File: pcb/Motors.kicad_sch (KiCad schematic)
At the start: 10 parts, among them M1 LEFT, M2 RIGHT, U11 TB6612FNG

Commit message: [pcb] 4 layer PCB
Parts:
- renumbered U11 to U12
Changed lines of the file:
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@@
   (symbol (lib_id "power:+3.3V") (at 46.99 58.42 0) (unit 1)
     (in_bom yes) (on_board yes) (dnp no) (fields_autoplaced)
-    (property "Reference" "#PWR042" (at 46.99 62.23 0)
+    (property "Reference" "#PWR043" (at 46.99 62.23 0)
       (effects (font (size 1.27 1.27)) hide)
     )
@@
       (project "Autko"
         (path "/8d5cfdec-de34-4148-9100-7125640c46f5/541574ca-21e4-445f-b8e2-ded2c59d3b8a"
-          (reference "#PWR042") (unit 1)
+          (reference "#PWR043") (unit 1)
         )
       )
@@
   (symbol (lib_id "Driver_Motor:TB6612FNG") (at 64.77 69.85 0) (unit 1)
     (in_bom yes) (on_board yes) (dnp no) (fields_autoplaced)
-    (property "Reference" "U11" (at 74.3459 92.71 0)
+    (property "Reference" "U12" (at 74.3459 92.71 0)
       (effects (font (size 1.27 1.27)) (justify left))
     )
@@
       (project "Autko"
         (path "/8d5cfdec-de34-4148-9100-7125640c46f5/541574ca-21e4-445f-b8e2-ded2c59d3b8a"
-          (reference "U11") (unit 1)
+          (reference "U12") (unit 1)
         )
       )
@@
   (symbol (lib_id "power:GND") (at 90.17 44.45 0) (unit 1)
     (in_bom yes) (on_board yes) (dnp no)
-    (property "Reference" "#PWR041" (at 90.17 50.8 0)
+    (property "Reference" "#PWR042" (at 90.17 50.8 0)
       (effects (font (size 1.27 1.27)) hide)
     )
@@
       (project "Autko"
         (path "/8d5cfdec-de34-4148-9100-7125640c46f5/541574ca-21e4-445f-b8e2-ded2c59d3b8a"
+          (reference "#PWR042") (unit 1)
+        )
+      )
+    )
+  )
+  (symbol (lib_id "power:+3.3V") (at 46.99 31.75 0) (unit 1)
+    (in_bom yes) (on_board yes) (dnp no) (fields_autoplaced)
+    (property "Reference" "#PWR039" (at 46.99 35.56 0)
+      (effects (font (size 1.27 1.27)) hide)
+    )
+    (property "Value" "+3.3V" (at 46.99 27.94 0)
+      (effects (font (size 1.27 1.27)))
+    )
+    (property "Footprint" "" (at 46.99 31.75 0)
+      (effects (font (size 1.27 1.27)) hide)
+    )
+    (property "Datasheet" "" (at 46.99 31.75 0)
+      (effects (font (size 1.27 1.27)) hide)
+    )
+    (pin "1")
+    (instances
+      (project "Autko"
+        (path "/8d5cfdec-de34-4148-9100-7125640c46f5/541574ca-21e4-445f-b8e2-ded2c59d3b8a"
+          (reference "#PWR039") (unit 1)
+        )
+      )
+    )
+  )
+  (symbol (lib_id "power:+7.5V") (at 90.17 31.75 0) (unit 1)
+    (in_bom yes) (on_board yes) (dnp no) (fields_autoplaced)
+    (property "Reference" "#PWR040" (at 90.17 35.56 0)
+      (effects (font (size 1.27 1.27)) hide)
+    )
+    (property "Value" "+7.5V" (at 90.17 27.94 0)
+      (effects (font (size 1.27 1.27)))
+    )
+    (property "Footprint" "" (at 90.17 31.75 0)
+      (effects (font (size 1.27 1.27)) hide)
+    )
+    (property "Datasheet" "" (at 90.17 31.75 0)
+      (effects (font (size 1.27 1.27)) hide)
+    )
+    (pin "1")
+    (instances
+      (project "Autko"
+        (path "/8d5cfdec-de34-4148-9100-7125640c46f5/541574ca-21e4-445f-b8e2-ded2c59d3b8a"
+          (reference "#PWR040") (unit 1)
+        )
+      )
+    )
+  )
+  (symbol (lib_id "Device:C") (at 92.71 59.69 0) (mirror y) (unit 1)
+    (in_bom yes) (on_board yes) (dnp no)
+    (property "Reference" "C22" (at 90.17 58.42 0)
+      (effects (font (size 1.27 1.27)) (justify left))
+    )
+    (property "Value" "100nF" (at 90.17 60.96 0)
+      (effects (font (size 1.27 1.27)) (justify left))
+    )
+    (property "Footprint" "Capacitor_SMD:C_0805_2012Metric" (at 91.7448 63.5 0)
+      (effects (font (size 1.27 1.27)) hide)
+    )
+    (property "Datasheet" "~" (at 92.71 59.69 0)
+      (effects (font (size 1.27 1.27)) hide)
+    )
+    (pin "1")
+    (pin "2")
+    (instances
+      (project "Autko"
+        (path "/8d5cfdec-de34-4148-9100-7125640c46f5/541574ca-21e4-445f-b8e2-ded2c59d3b8a"
+          (reference "C22") (unit 1)
+        )
+      )
+    )
+  )
+  (symbol (lib_id "Device:C") (at 77.47 38.1 0) (unit 1)
+    (in_bom yes) (on_board yes) (dnp no)
+    (property "Reference" "C20" (at 80.01 36.83 0)
+      (effects (font (size 1.27 1.27)) (justify left))
+    )
+    (property "Value" "100nF" (at 80.01 39.37 0)
+      (effects (font (size 1.27 1.27)) (justify left))
+    )
+    (property "Footprint" "Capacitor_SMD:C_0805_2012Metric" (at 78.4352 41.91 0)
+      (effects (font (size 1.27 1.27)) hide)
+    )
+    (property "Datasheet" "~" (at 77.47 38.1 0)
+      (effects (font (size 1.27 1.27)) hide)
+    )
+    (pin "1")
+    (pin "2")
+    (instances
+      (project "Autko"
+        (path "/8d5cfdec-de34-4148-9100-7125640c46f5/541574ca-21e4-445f-b8e2-ded2c59d3b8a"
+          (reference "C20") (unit 1)
+        )
+      )
+    )
+  )
+  (symbol (lib_id "power:GND") (at 46.99 44.45 0) (unit 1)
+    (in_bom yes) (on_board yes) (dnp no)
+    (property "Reference" "#PWR041" (at 46.99 50.8 0)
+      (effects (font (size 1.27 1.27)) hide)
+    )
+    (property "Value" "GND" (at 46.99 48.26 0)
+      (effects (font (size 1.27 1.27)))
+    )
+    (property "Footprint" "" (at 46.99 44.45 0)
+      (effects (font (size 1.27 1.27)) hide)
+    )
+    (property "Datasheet" "" (at 46.99 44.45 0)
+      (effects (font (size 1.27 1.27)) hide)
+    )
+    (pin "1")
+    (instances
+      (project "Autko"
+        (path "/8d5cfdec-de34-4148-9100-7125640c46f5/541574ca-21e4-445f-b8e2-ded2c59d3b8a"
           (reference "#PWR041") (unit 1)
         )
@@
     )
   )
-  (symbol (lib_id "power:+3.3V") (at 46.99 31.75 0) (unit 1)
-    (in_bom yes) (on_board yes) (dnp no) (fields_autoplaced)
-    (property "Reference" "#PWR038" (at 46.99 35.56 0)
-      (effects (font (size 1.27 1.27)) hide)
-    )
-    (property "Value" "+3.3V" (at 46.99 27.94 0)
-      (effects (font (size 1.27 1.27)))
-    )
-    (property "Footprint" "" (at 46.99 31.75 0)
-      (effects (font (size 1.27 1.27)) hide)
-    )
-    (property "Datasheet" "" (at 46.99 31.75 0)
-      (effects (font (size 1.27 1.27)) hide)
-    )
-    (pin "1")
-    (instances
-      (project "Autko"
-        (path "/8d5cfdec-de34-4148-9100-7125640c46f5/541574ca-21e4-445f-b8e2-ded2c59d3b8a"
-          (reference "#PWR038") (unit 1)
-        )
-      )
-    )
-  )
-  (symbol (lib_id "power:+7.5V") (at 90.17 31.75 0) (unit 1)
-    (in_bom yes) (on_board yes) (dnp no) (fields_autoplaced)
-    (property "Reference" "#PWR039" (at 90.17 35.56 0)
-      (effects (font (size 1.27 1.27)) hide)
-    )
-    (property "Value" "+7.5V" (at 90.17 27.94 0)
-      (effects (font (size 1.27 1.27)))
-    )
-    (property "Footprint" "" (at 90.17 31.75 0)
-      (effects (font (size 1.27 1.27)) hide)
-    )
-    (property "Datasheet" "" (at 90.17 31.75 0)
-      (effects (font (size 1.27 1.27)) hide)
-    )
-    (pin "1")
-    (instances
-      (project "Autko"
-        (path "/8d5cfdec-de34-4148-9100-7125640c46f5/541574ca-21e4-445f-b8e2-ded2c59d3b8a"
-          (reference "#PWR039") (unit 1)
-        )
-      )
-    )
-  )
-  (symbol (lib_id "Device:C") (at 92.71 59.69 0) (mirror y) (unit 1)
-    (in_bom yes) (on_board yes) (dnp no)
-    (property "Reference" "C22" (at 90.17 58.42 0)
-      (effects (font (size 1.27 1.27)) (justify left))
-    )
-    (property "Value" "100nF" (at 90.17 60.96 0)
-      (effects (font (size 1.27 1.27)) (justify left))
-    )
-    (property "Footprint" "Capacitor_SMD:C_0805_2012Metric" (at 91.7448 63.5 0)
-      (effects (font (size 1.27 1.27)) hide)
-    )
-    (property "Datasheet" "~" (at 92.71 59.69 0)
-      (effects (font (size 1.27 1.27)) hide)
-    )
-    (pin "1")
-    (pin "2")
-    (instances
-      (project "Autko"
-        (path "/8d5cfdec-de34-4148-9100-7125640c46f5/541574ca-21e4-445f-b8e2-ded2c59d3b8a"
-          (reference "C22") (unit 1)
-        )
-      )
-    )
-  )
-  (symbol (lib_id "Device:C") (at 77.47 38.1 0) (unit 1)
-    (in_bom yes) (on_board yes) (dnp no)
-    (property "Reference" "C20" (at 80.01 36.83 0)
-      (effects (font (size 1.27 1.27)) (justify left))
-    )
-    (property "Value" "100nF" (at 80.01 39.37 0)
-      (effects (font (size 1.27 1.27)) (justify left))
-    )
-    (property "Footprint" "Capacitor_SMD:C_0805_2012Metric" (at 78.4352 41.91 0)
-      (effects (font (size 1.27 1.27)) hide)
-    )
-    (property "Datasheet" "~" (at 77.47 38.1 0)
-      (effects (font (size 1.27 1.27)) hide)
-    )
-    (pin "1")
-    (pin "2")
-    (instances
-      (project "Autko"
-        (path "/8d5cfdec-de34-4148-9100-7125640c46f5/541574ca-21e4-445f-b8e2-ded2c59d3b8a"
-          (reference "C20") (unit 1)
-        )
-      )
-    )
-  )
-  (symbol (lib_id "power:GND") (at 46.99 44.45 0) (unit 1)
-    (in_bom yes) (on_board yes) (dnp no)
-    (property "Reference" "#PWR040" (at 46.99 50.8 0)
-      (effects (font (size 1.27 1.27)) hide)
-    )
-    (property "Value" "GND" (at 46.99 48.26 0)
-      (effects (font (size 1.27 1.27)))
-    )
-    (property "Footprint" "" (at 46.99 44.45 0)
-      (effects (font (size 1.27 1.27)) hide)
-    )
-    (property "Datasheet" "" (at 46.99 44.45 0)
-      (effects (font (size 1.27 1.27)) hide)
-    )
-    (pin "1")
-    (instances
-      (project "Autko"
-        (path "/8d5cfdec-de34-4148-9100-7125640c46f5/541574ca-21e4-445f-b8e2-ded2c59d3b8a"
-          (reference "#PWR040") (unit 1)
-        )
-      )
-    )
-  )
   (symbol (lib_id "power:GND") (at 67.31 97.79 0) (unit 1)
     (in_bom yes) (on_board yes) (dnp no)
-    (property "Reference" "#PWR043" (at 67.31 104.14 0)
+    (property "Reference" "#PWR044" (at 67.31 104.14 0)
       (effects (font (size 1.27 1.27)) hide)
     )
@@
       (project "Autko"
         (path "/8d5cfdec-de34-4148-9100-7125640c46f5/541574ca-21e4-445f-b8e2-ded2c59d3b8a"
-          (reference "#PWR043") (unit 1)
-        )
-      )
+          (reference "#PWR044") (unit 1)
+        )
+      )

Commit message: [pcb] BT config rework
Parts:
- renumbered TP15 to TP14, TP16 to TP15, U12 to U11
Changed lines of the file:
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@@
   (symbol (lib_id "Connector:TestPoint") (at 35.56 68.58 180) (unit 1)
     (in_bom yes) (on_board yes) (dnp no)
-    (property "Reference" "TP16" (at 35.56 73.66 0)
+    (property "Reference" "TP15" (at 35.56 73.66 0)
       (effects (font (size 1.27 1.27)))
     )
@@
       (project "Autko"
         (path "/8d5cfdec-de34-4148-9100-7125640c46f5/541574ca-21e4-445f-b8e2-ded2c59d3b8a"
-          (reference "TP16") (unit 1)
+          (reference "TP15") (unit 1)
         )
       )
@@
   (symbol (lib_id "Connector:TestPoint") (at 35.56 63.5 0) (unit 1)
     (in_bom yes) (on_board yes) (dnp no)
-    (property "Reference" "TP15" (at 35.56 58.42 0)
+    (property "Reference" "TP14" (at 35.56 58.42 0)
       (effects (font (size 1.27 1.27)))
     )
@@
       (project "Autko"
         (path "/8d5cfdec-de34-4148-9100-7125640c46f5/541574ca-21e4-445f-b8e2-ded2c59d3b8a"
-          (reference "TP15") (unit 1)
+          (reference "TP14") (unit 1)
         )
       )
@@
   (symbol (lib_id "power:+3.3V") (at 46.99 58.42 0) (unit 1)
     (in_bom yes) (on_board yes) (dnp no) (fields_autoplaced)
-    (property "Reference" "#PWR043" (at 46.99 62.23 0)
+    (property "Reference" "#PWR048" (at 46.99 62.23 0)
       (effects (font (size 1.27 1.27)) hide)
     )
@@
       (project "Autko"
         (path "/8d5cfdec-de34-4148-9100-7125640c46f5/541574ca-21e4-445f-b8e2-ded2c59d3b8a"
-          (reference "#PWR043") (unit 1)
+          (reference "#PWR048") (unit 1)
         )
       )
@@
   (symbol (lib_id "Driver_Motor:TB6612FNG") (at 64.77 69.85 0) (unit 1)
     (in_bom yes) (on_board yes) (dnp no) (fields_autoplaced)
-    (property "Reference" "U12" (at 74.3459 92.71 0)
+    (property "Reference" "U11" (at 74.3459 92.71 0)
       (effects (font (size 1.27 1.27)) (justify left))
     )
@@
       (project "Autko"
         (path "/8d5cfdec-de34-4148-9100-7125640c46f5/541574ca-21e4-445f-b8e2-ded2c59d3b8a"
-          (reference "U12") (unit 1)
+          (reference "U11") (unit 1)
         )
       )
@@
   (symbol (lib_id "power:GND") (at 90.17 44.45 0) (unit 1)
     (in_bom yes) (on_board yes) (dnp no)
-    (property "Reference" "#PWR042" (at 90.17 50.8 0)
+    (property "Reference" "#PWR047" (at 90.17 50.8 0)
       (effects (font (size 1.27 1.27)) hide)
     )
@@
       (project "Autko"
         (path "/8d5cfdec-de34-4148-9100-7125640c46f5/541574ca-21e4-445f-b8e2-ded2c59d3b8a"
-          (reference "#PWR042") (unit 1)
+          (reference "#PWR047") (unit 1)
         )
       )
@@
   (symbol (lib_id "power:+3.3V") (at 46.99 31.75 0) (unit 1)
     (in_bom yes) (on_board yes) (dnp no) (fields_autoplaced)
-    (property "Reference" "#PWR039" (at 46.99 35.56 0)
+    (property "Reference" "#PWR044" (at 46.99 35.56 0)
       (effects (font (size 1.27 1.27)) hide)
     )
@@
       (project "Autko"
         (path "/8d5cfdec-de34-4148-9100-7125640c46f5/541574ca-21e4-445f-b8e2-ded2c59d3b8a"
-          (reference "#PWR039") (unit 1)
+          (reference "#PWR044") (unit 1)
         )
       )
@@
   (symbol (lib_id "power:+7.5V") (at 90.17 31.75 0) (unit 1)
     (in_bom yes) (on_board yes) (dnp no) (fields_autoplaced)
-    (property "Reference" "#PWR040" (at 90.17 35.56 0)
+    (property "Reference" "#PWR045" (at 90.17 35.56 0)
       (effects (font (size 1.27 1.27)) hide)
     )
@@
       (project "Autko"
         (path "/8d5cfdec-de34-4148-9100-7125640c46f5/541574ca-21e4-445f-b8e2-ded2c59d3b8a"
-          (reference "#PWR040") (unit 1)
+          (reference "#PWR045") (unit 1)
         )
       )
@@
   (symbol (lib_id "power:GND") (at 46.99 44.45 0) (unit 1)
     (in_bom yes) (on_board yes) (dnp no)
-    (property "Reference" "#PWR041" (at 46.99 50.8 0)
+    (property "Reference" "#PWR046" (at 46.99 50.8 0)
       (effects (font (size 1.27 1.27)) hide)
     )
@@
       (project "Autko"
         (path "/8d5cfdec-de34-4148-9100-7125640c46f5/541574ca-21e4-445f-b8e2-ded2c59d3b8a"
-          (reference "#PWR041") (unit 1)
+          (reference "#PWR046") (unit 1)
         )
       )
@@
   (symbol (lib_id "power:GND") (at 67.31 97.79 0) (unit 1)
     (in_bom yes) (on_board yes) (dnp no)
-    (property "Reference" "#PWR044" (at 67.31 104.14 0)
+    (property "Reference" "#PWR049" (at 67.31 104.14 0)
       (effects (font (size 1.27 1.27)) hide)
     )
@@
       (project "Autko"
         (path "/8d5cfdec-de34-4148-9100-7125640c46f5/541574ca-21e4-445f-b8e2-ded2c59d3b8a"
-          (reference "#PWR044") (unit 1)
-        )
-      )
+          (reference "#PWR049") (unit 1)
+        )
+      )

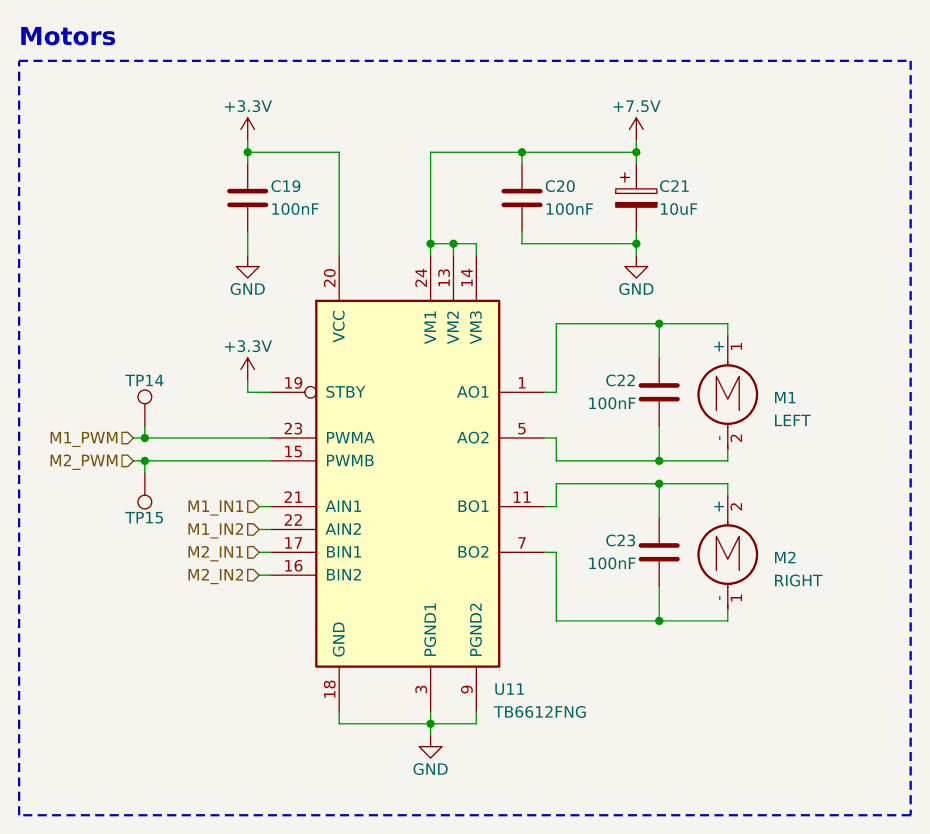
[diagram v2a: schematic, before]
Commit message: [pcb] More final touches, UART test ponts added.
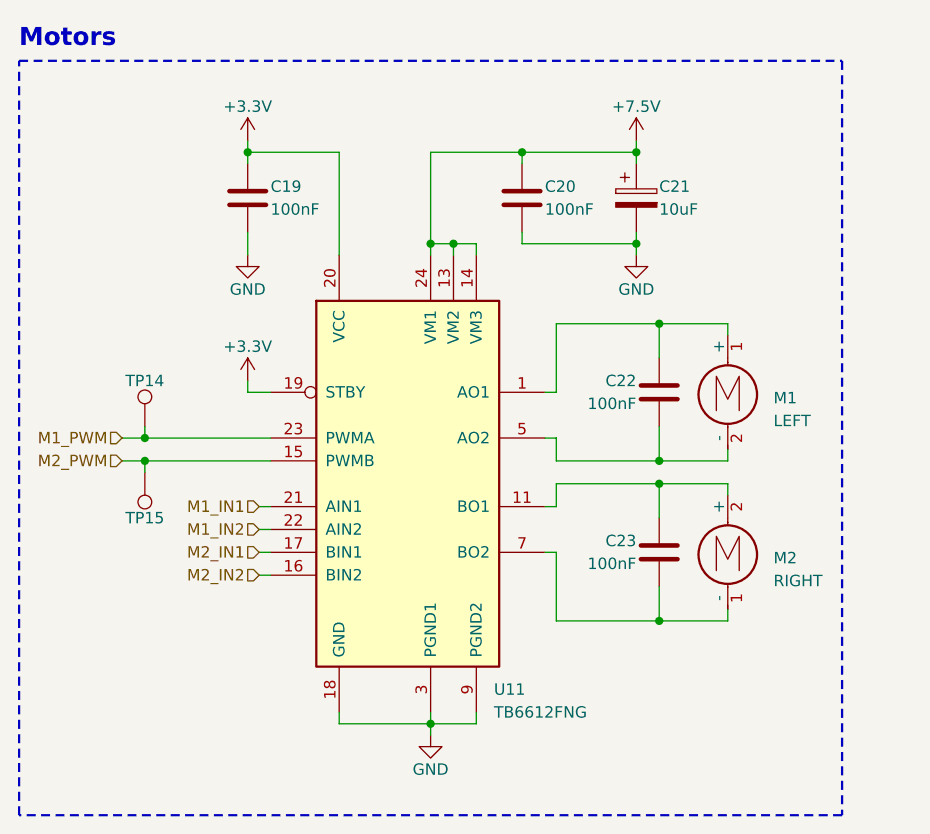
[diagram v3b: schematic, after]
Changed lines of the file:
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@@
     (stroke (width 0) (type default))
   )
-  (wire (pts (xy 34.29 67.31) (xy 35.56 67.31))
+  (wire (pts (xy 33.02 67.31) (xy 35.56 67.31))
     (stroke (width 0) (type default))
   )
@@
     (stroke (width 0) (type default))
   )
-  (wire (pts (xy 34.29 64.77) (xy 35.56 64.77))
+  (wire (pts (xy 33.02 64.77) (xy 35.56 64.77))
     (stroke (width 0) (type default))
   )
@@
     (stroke (width 0) (type default))
   )
-  (rectangle (start 21.59 22.86) (end 120.65 106.68)
+  (rectangle (start 21.59 22.86) (end 113.03 106.68)
     (stroke (width 0.25) (type dash))
     (fill (type none))
@@
     (effects (font (size 1.27 1.27)) (justify right))
   )
-  (hierarchical_label "M2_PWM" (shape input) (at 34.29 67.31 180) (fields_autoplaced)
+  (hierarchical_label "M2_PWM" (shape input) (at 33.02 67.31 180) (fields_autoplaced)
     (effects (font (size 1.27 1.27)) (justify right))
   )
@@
     (effects (font (size 1.27 1.27)) (justify right))
   )
-  (hierarchical_label "M1_PWM" (shape input) (at 34.29 64.77 180) (fields_autoplaced)
+  (hierarchical_label "M1_PWM" (shape input) (at 33.02 64.77 180) (fields_autoplaced)
     (effects (font (size 1.27 1.27)) (justify right))
   )

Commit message: [pcb] 10uF capacitor changed from A to T package
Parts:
- C21: footprint Capacitor_Tantalum_SMD:CP_EIA-3216-18_Kemet-A -> Capacitor_Tantalum_SMD:CP_EIA-3528-12_Kemet-T
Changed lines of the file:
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@@
       (effects (font (size 1.27 1.27)) (justify left))
     )
-    (property "Footprint" "Capacitor_Tantalum_SMD:CP_EIA-3216-18_Kemet-A" (at 91.1352 41.91 0)
+    (property "Footprint" "Capacitor_Tantalum_SMD:CP_EIA-3528-12_Kemet-T" (at 91.1352 41.91 0)
       (effects (font (size 1.27 1.27)) hide)
     )
